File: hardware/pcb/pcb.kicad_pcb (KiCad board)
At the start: 2 copper layers, 88 x 53 mm, 40 parts, among them J1 TYPE-C-31-M-12, Q1 FDN339AN, SW1 SW_SPST, U1 WeMos_D1_mini, U2 TSOP38236, U3 MCP73831-2-OT, U4 BQ27441DRZR-G1A, U5 TLV75733PDBV

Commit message: Added schematic
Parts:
- BT1: value LiPo cell -> protected 18650
- renumbered R15 to R12, R12 to R13, R13 to R14, R14 to R15
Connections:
- net /IR_DeMod_VCC renamed IR_RECV_VCC
- net /Power management/SCL renamed SCL
- net /Power management/SDA renamed SDA
- net /Power management/~LOW_BAT renamed ~LOW_BAT
- net /device_wake renamed device_wake
- net /factory_reset renamed factory_rst
- net /~RST renamed ~RST
- R15 pad 2: +1V8 -> +3V3
- U1 pad 11: /IR_DeMod_SIG -> IR_SIGNAL
- U1 pad 4: /IR_BLASTER -> IR_BLAST
- U2 pad 1: /IR_DEMOD_SIG -> IR_SIGNAL
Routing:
- net IR_SIGNAL: track 0.00 -> 22.4 mm
- net +1V8: track 17.6 -> 6.53 mm, vias 2 -> 1
- net +3V3: track 145.2 -> 152.3 mm
- net ~LOW_BAT: track 70.3 -> 67.6 mm
- net SDA: track 40.8 -> 40.3 mm
- net GND: vias 83 -> 88
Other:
- board text added: "JLCJLCJLCJLC"

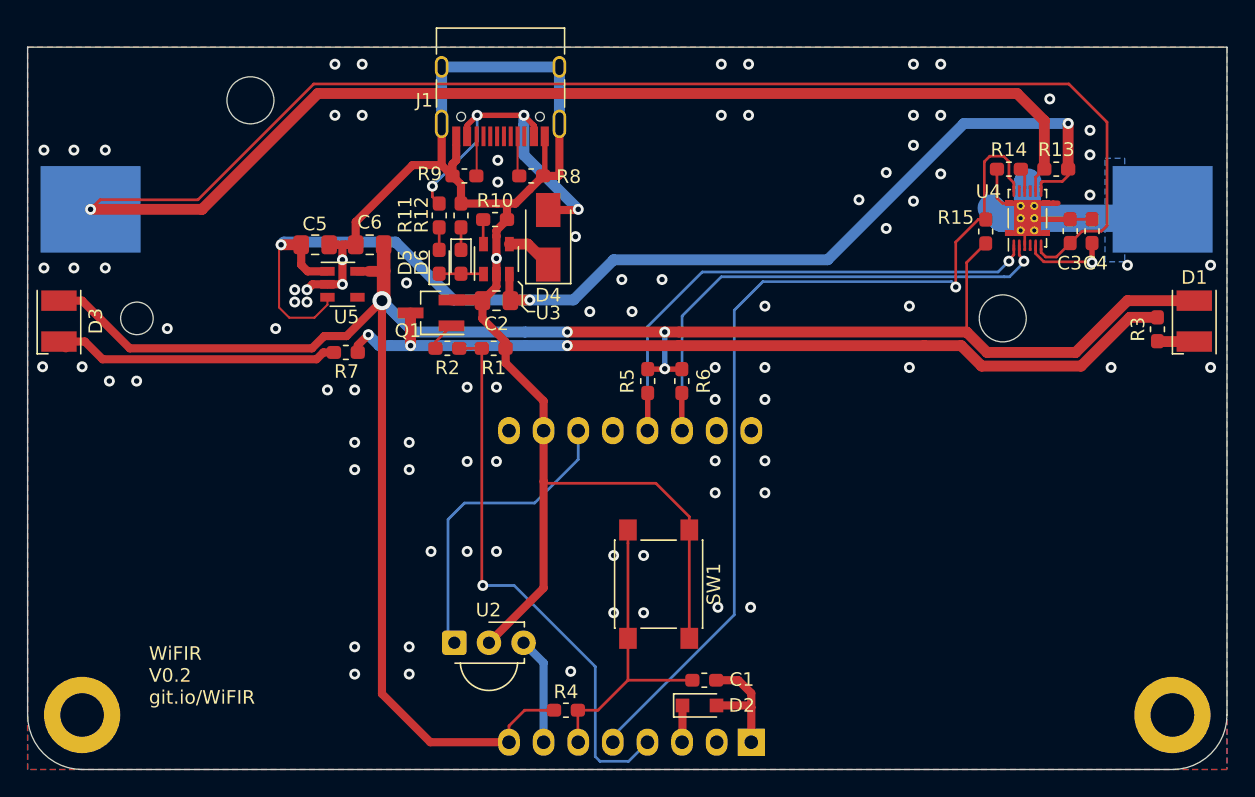
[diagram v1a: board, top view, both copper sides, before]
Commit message: Centered USB-C, Added cutouts for 15mm case posts
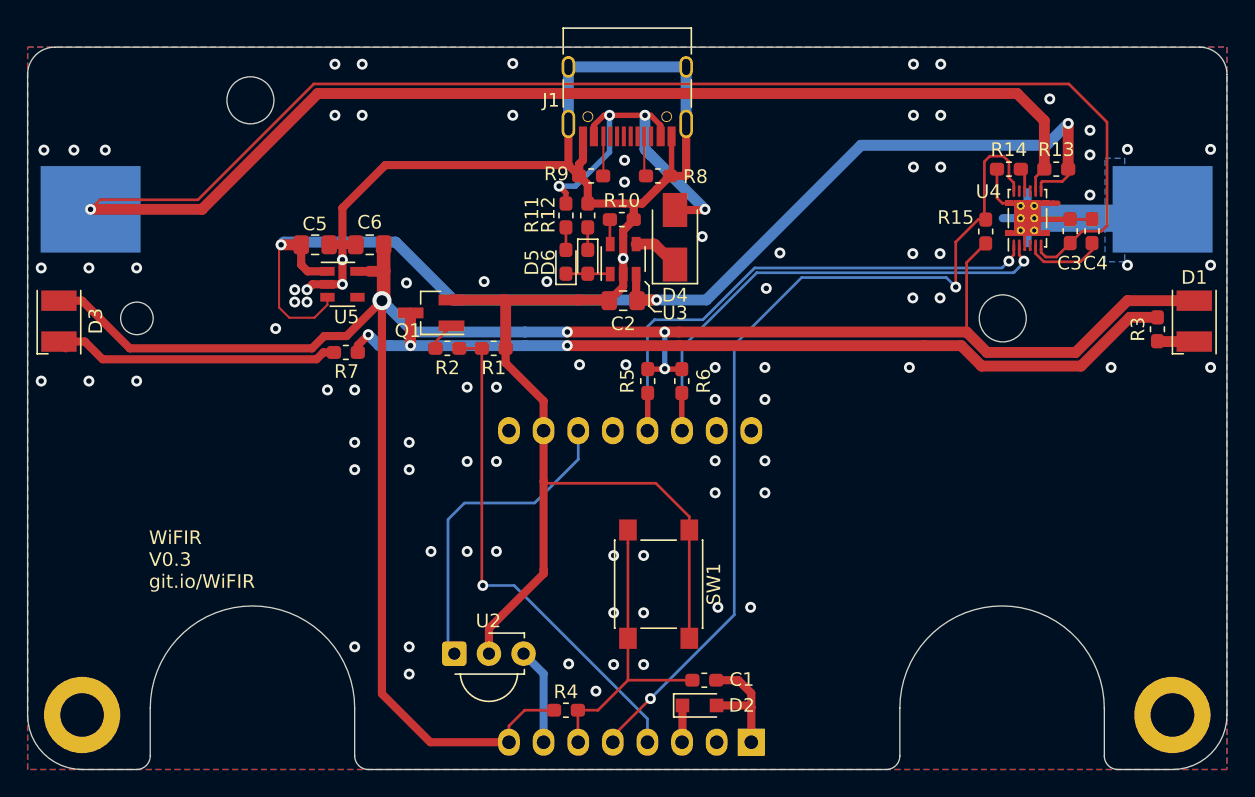
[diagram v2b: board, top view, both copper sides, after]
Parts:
- moved D4 9.30 mm to (221.5, 78.0)
- moved D5 9.30 mm to (213.5, 79.8)
- moved J1 9.30 mm to (218.0, 66.5)
- moved R11 9.30 mm to (213.5, 76.3)
- moved R8 9.30 mm to (220.2, 73.5)
- moved C2 9.30 mm to (217.7, 82.6)
- moved D6 9.30 mm to (215.1, 79.8)
- moved R10 9.30 mm to (217.6, 76.7)
- moved R12 9.30 mm to (215.1, 76.3)
- moved R9 9.30 mm to (215.3, 73.5)
- moved U3 9.30 mm to (217.7, 79.5)
- moved G*** 8.50 mm to (189.2, 92.7)
- moved G*** 8.50 mm to (185.2, 92.7)
- moved U2 0.80 mm to (205.3, 108.5)
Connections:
- R1 pad 2: /IR_BLASTER -> IR_BLAST
- R2 pad 1: /IR_BLASTER -> IR_BLAST
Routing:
- net /IR_BLASTER: track 41.0 -> 0.00 mm, vias 1 -> 0
- net IR_BLAST: track 0.00 -> 36.9 mm, vias 0 -> 1
- net GND: track 149.5 -> 169.8 mm
- net SCL: track 39.4 -> 38.0 mm
- net IR_SIGNAL: track 22.4 -> 23.5 mm
- net VBUS: track 26.2 -> 27.2 mm
- net IR_RECV_VCC: track 7.91 -> 7.11 mm
- net ~LOW_BAT: track 67.6 -> 66.9 mm, vias 1 -> 2
- net +1V8: track 6.53 -> 5.89 mm, vias 1 -> 0
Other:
- outline, holes or cut-outs redrawn
- board text added: "WiFIR V0.3 git.io/WiFIR"
- board text removed: "WiFIR V0.2 git.io/WiFIR"
